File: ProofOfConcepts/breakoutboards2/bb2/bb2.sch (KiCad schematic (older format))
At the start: 11 parts, among them J1 Conn_01x03_Female, U1 PAM2305CGFADJ

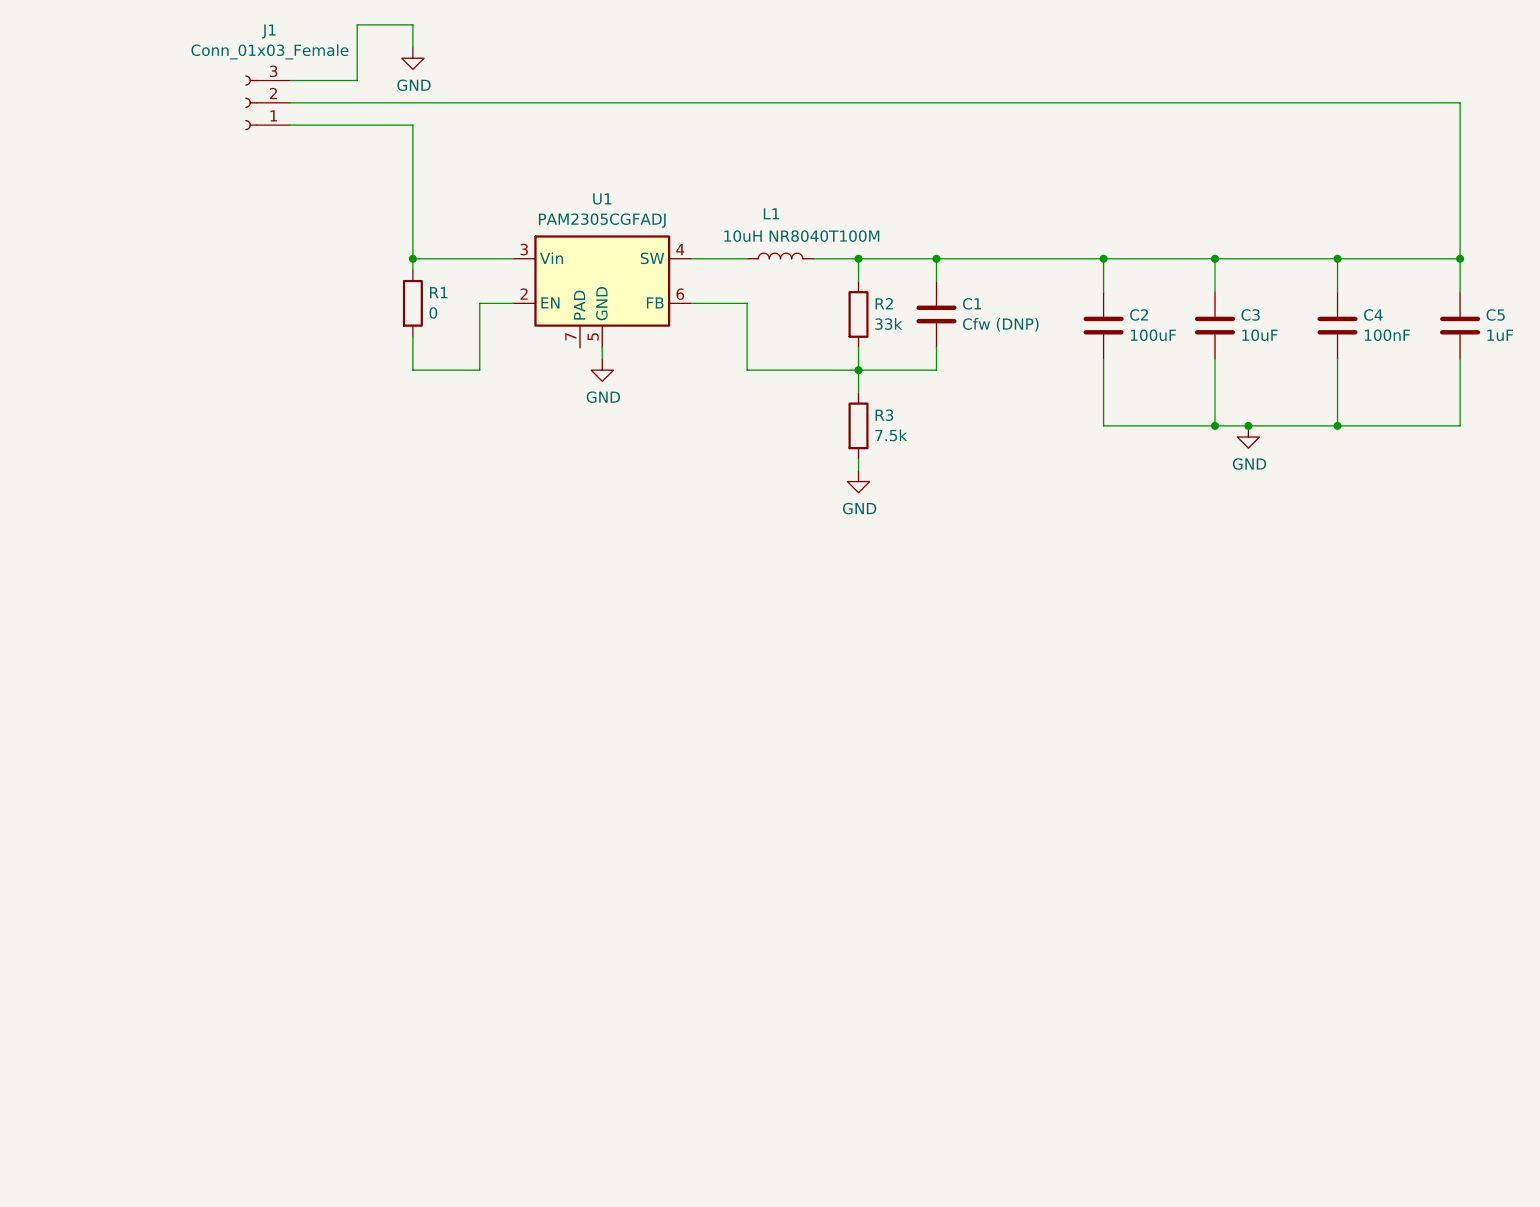
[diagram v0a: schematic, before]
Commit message: breakout board for v2 buck and nmos driver
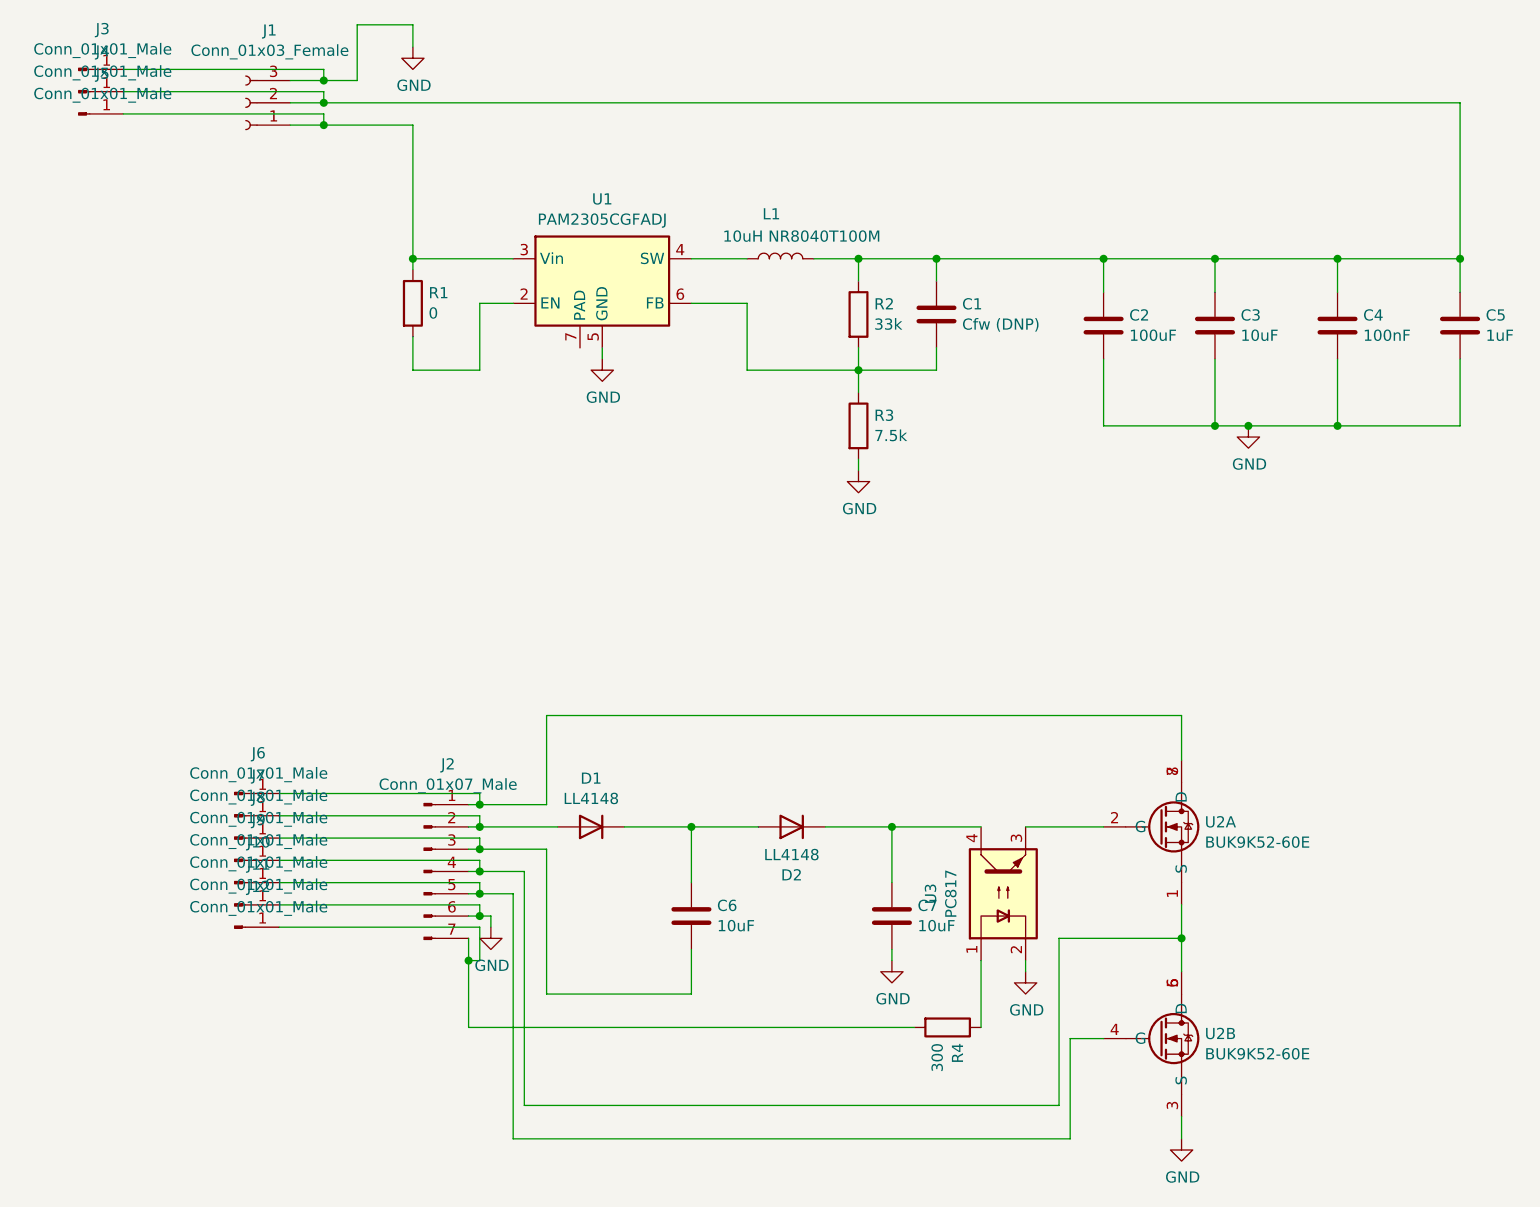
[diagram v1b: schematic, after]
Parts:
- added C6, C7: 10uF, Capacitor_SMD:C_0805_2012Metric_Pad1.18x1.45mm_HandSolder, symbol Device:C
- added D1, D2: LL4148, Diode_SMD:D_MiniMELF, symbol Diode:LL4148
- added J10, J11, J12, J3, J4, J5, J6, J7, J8, J9: Conn_01x01_Male, 1KicadLib:GatorTestpoint, symbol Connector:Conn_01x01_Male
- added J2: Conn_01x07_Male, Connector_PinHeader_2.54mm:PinHeader_1x07_P2.54mm_Vertical, symbol Connector:Conn_01x07_Male
- added R4: 300, Resistor_SMD:R_0805_2012Metric_Pad1.20x1.40mm_HandSolder, symbol Device:R
- added U2: BUK9K52-60E, 1KicadLib:LFPAK56D, symbol 1KicadLib:BUK9K52-60E
- added U3: PC817, Package_SO:SOP-4_3.8x4.1mm_P2.54mm, symbol Isolator:PC817
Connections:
- net GND: now also C7.2, J11.1 (Pin_1), J2.6 (Pin_6), J3.1 (Pin_1), U2.3 (S), U3.2
- net at J1.1 (Pin_1), R1.1, U1.3 (Vin): now also J5.1 (Pin_1)
- net at C1.1, C2.1, C3.1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: now also J4.1 (Pin_1)
- new net: J2.4 (Pin_4), J9.1 (Pin_1), U2.1 (S), U2.5 (D), U2.6 (D)
- new net: U2.2 (G), U3.3
- new net: J2.1 (Pin_1), J6.1 (Pin_1), U2.7 (D), U2.8 (D)
- new net: J10.1 (Pin_1), J2.5 (Pin_5), U2.4 (G)
- new net: C6.1, D1.1 (K), D2.2 (A)
- new net: D1.2 (A), J2.2 (Pin_2), J7.1 (Pin_1)
- new net: C6.2, J2.3 (Pin_3), J8.1 (Pin_1)
- new net: C7.1, D2.1 (K), U3.4
- new net: J12.1 (Pin_1), J2.7 (Pin_7), R4.2
- new net: R4.1, U3.1
